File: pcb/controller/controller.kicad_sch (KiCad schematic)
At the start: 0 parts

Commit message: Started controller schematic
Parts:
- added C1: 22uF, symbol Device:C
- added C12, C2, C4: 0.1uF, symbol Device:C
- added C3: 1uF, symbol Device:C
- added J1: UART, symbol Connector:Conn_01x04_Pin
- added R1, R15, R2: 10kR, symbol Device:R
- added SW1: HX TS3315A-H 250GF, lcsc:SW-SMD_4P-L3.4-W3.4-P2.00-LS4.0_TS3315A160GF, symbol lcsc:HXTS3315A-H250GF
- added SW2: Play, lcsc:KEY-SMD_4P-L4.2-W3.2-P2.20-LS4.6, symbol lcsc:SKRPACE010
- added SW3: Reset, lcsc:KEY-SMD_4P-L4.2-W3.2-P2.20-LS4.6, symbol lcsc:SKRPACE010
- added SW4: Pair, lcsc:KEY-SMD_4P-L4.2-W3.2-P2.20-LS4.6, symbol lcsc:SKRPACE010
- added U2: ESP32-C6-MINI-1, RF_Module:ESP32-C6-MINI-1, symbol RF_Module:ESP32-C6-MINI-1
- added U3: SP3485EN-L/TR, lcsc:SOIC-8_L5.0-W4.0-P1.27-LS6.0-BL, symbol lcsc:SP3485EN-L_TR
- added U7: GT36549, lcsc:RES-SMD_L3.6-W2.4, symbol lcsc:GT36549
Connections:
- new net: J1.3 (Pin_3), U2.30 (RXD0)
- new net: J1.2 (Pin_2), U2.31 (TXD0)
- new net: C4.2, SW1.4 (D)
- new net +3V3: C1.1, C2.1, J1.1 (Pin_1), R1.1, R2.1, U2.3 (3V3), U3.8 (VCC), U7.1
- new net A: U3.6 (A)
- new net B: U3.7 (B)
- new net DE: U3.3 (DE)
- new net EN: C3.1, C4.1, R1.2, SW1.2 (B), U2.8 (EN)
- new net GND: C1.2, C12.2, C2.2, C3.2, J1.4 (Pin_4), R15.2, SW1.3 (C), SW1.5 (GND), SW2.4, SW3.4, SW4.4, U2.1 (GND), U2.11 (GND), U2.14 (GND), U2.2 (GND), U2.36 (GND), U2.37 (GND), U2.38 (GND), U2.39 (GND), U2.40 (GND), U2.41 (GND), U2.42 (GND), U2.43 (GND), U2.44 (GND), U2.45 (GND), U2.46 (GND), U2.47 (GND), U2.48 (GND), U2.49 (GND), U2.50 (GND), U2.51 (GND), U2.52 (GND), U2.53 (GND), U3.5 (GND)
- new net IO8: R2.2, U2.22 (IO8)
- new net Light_sense: C12.1, R15.1, U7.2
- new net RE: U3.2 (~{RE})
- new net RX: U3.1 (RO)
- new net SW_Reset: SW3.1
- new net SW_pair: SW4.1
- new net SW_play: SW2.1
- new net TX: U3.4 (DI)
- new net USB_D+: U2.18 (IO13)
- new net USB_D-: U2.17 (IO12)
- no-connect marks 0 -> 7
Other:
- added sheet Power (power.kicad_sch)
- added sheet Segment Display (segment_display.kicad_sch)
- note added: "Buttons"
- note added: "MCU"
- note added: "Photoresistor"
- note added: "RS-485"
- note added: "TODO: Strapping pins"
- title: (none) -> BlitzPong-Controller

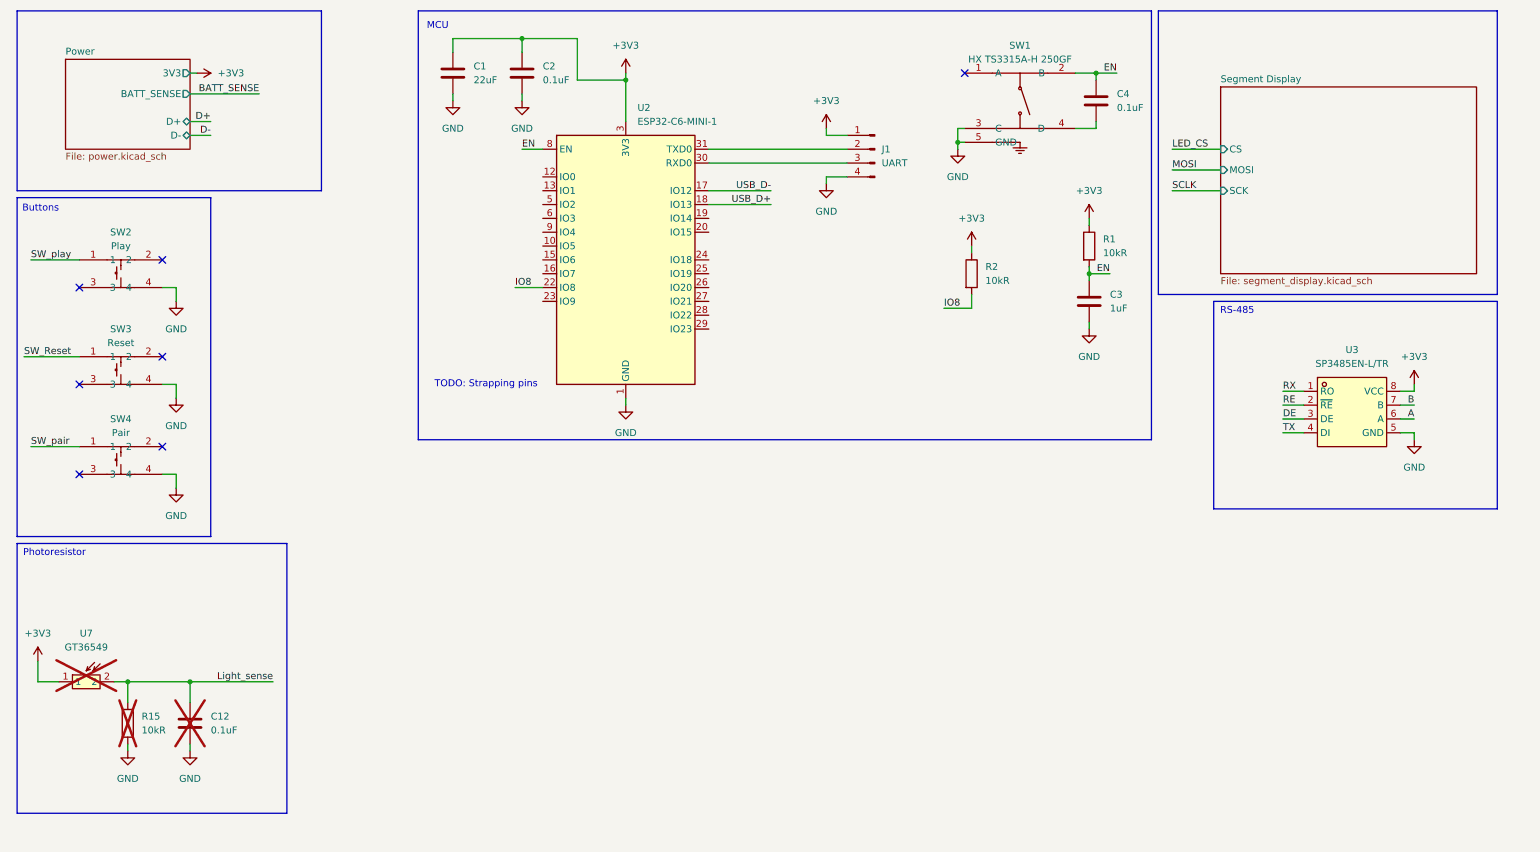
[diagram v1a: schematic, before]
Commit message: Added buzzer and connector to controller schematic
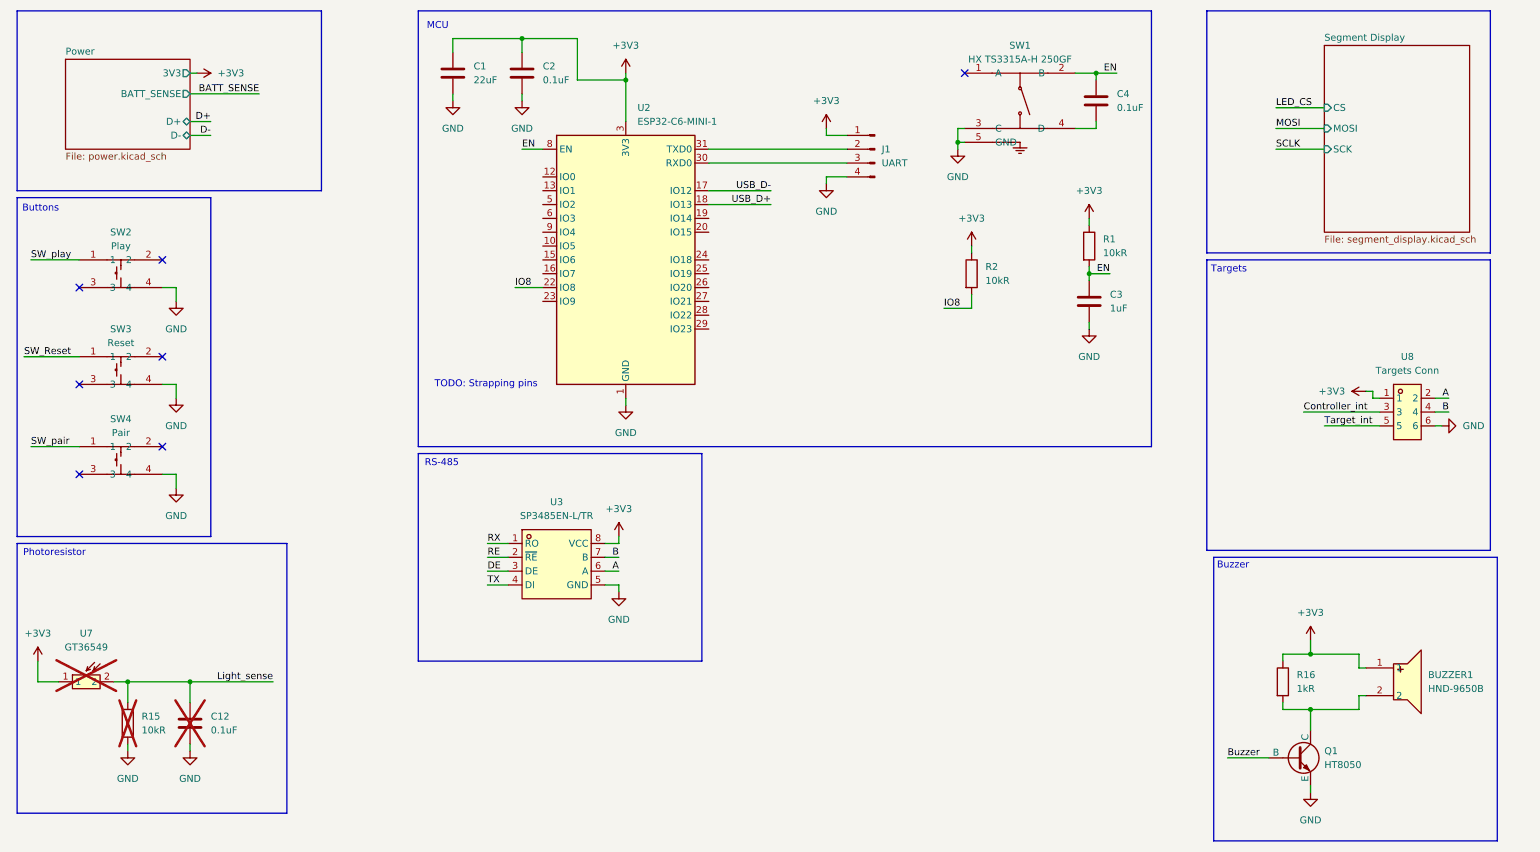
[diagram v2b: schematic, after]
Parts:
- added BUZZER1: HND-9650B, lcsc:BUZ-SMD_L9.6-W9.6-LS10.0-R, symbol lcsc:HND-9650B
- added Q1: HT8050, Package_TO_SOT_SMD:SOT-23-3, symbol Simulation_SPICE:NPN
- added R16: 1kR, symbol Device:R
- added U8: Targets Conn, lcsc:CONN-SMD_HC-PM254-5.0H-2X3PS-02A, symbol lcsc:HC-PM254-5.0H-2X3PS-02A
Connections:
- net +3V3: now also BUZZER1.1, R16.1, U8.1
- net A: now also U8.2
- net B: now also U8.4
- net GND: now also Q1.3 (E), U8.6
- new net: BUZZER1.2, Q1.1 (C), R16.2
- new net Buzzer: Q1.2 (B)
- new net Controller_int: U8.3
- new net Target_int: U8.5
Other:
- note added: "Buzzer"
- note added: "Targets"
- moved on the sheet: U3
